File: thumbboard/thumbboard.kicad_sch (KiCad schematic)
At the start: 9 parts, among them J1 Conn_01x05_MountingPin, SW1 SW_Push, SW2 SW_Push, SW3 SW_Push, SW4 SW_Push

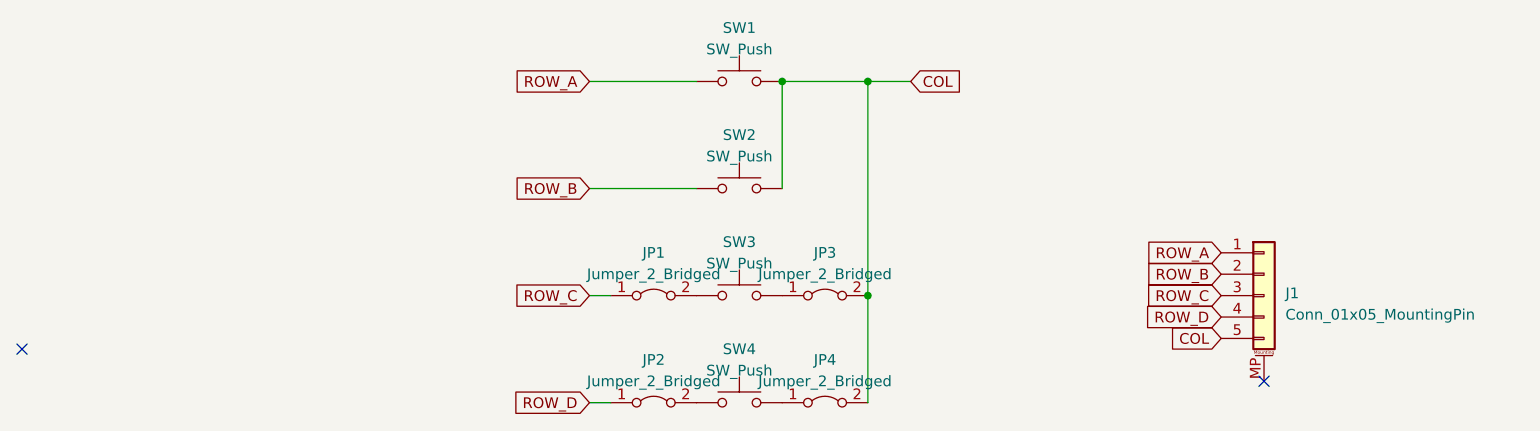
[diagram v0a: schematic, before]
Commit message: layout and cleanups (but J1 still in the wrong spot)
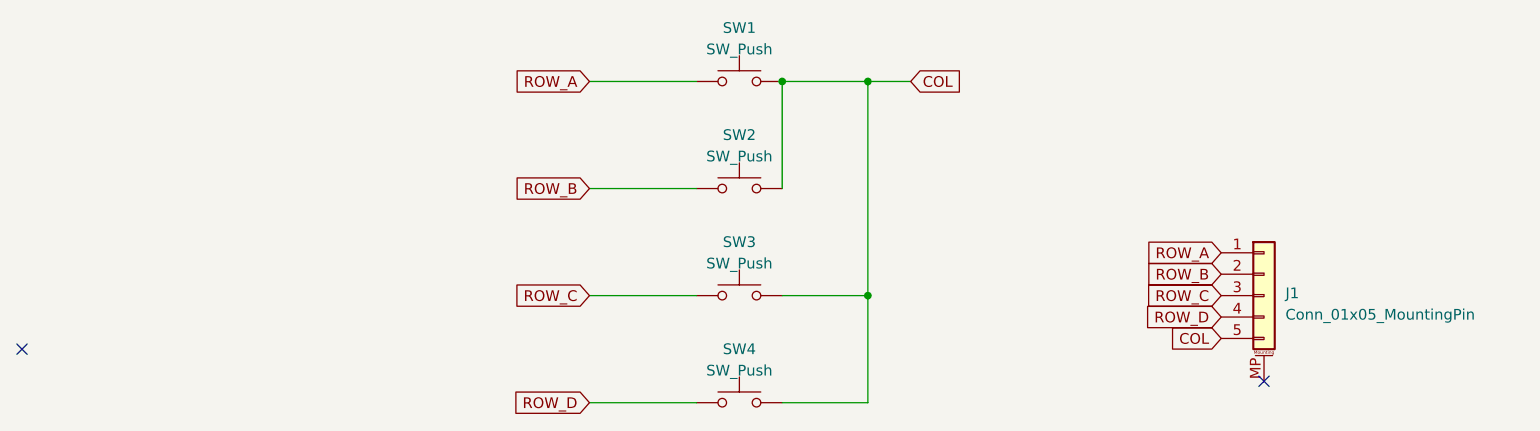
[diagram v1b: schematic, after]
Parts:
- removed JP1, JP2, JP3, JP4: Jumper_2_Bridged, symbol Jumper:Jumper_2_Bridged
- J1: footprint (none) -> Connector_FFC-FPC:Molex_200528-0050_1x05-1MP_P1.00mm_Horizontal
- SW1, SW2, SW3, SW4: footprint (none) -> keyswitches:SW_PG1350
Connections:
- net COL: now also SW1.1, SW3.2, SW4.2; no longer SW1.2
- net ROW_A: now also SW1.2; no longer SW1.1
- net ROW_C: now also SW3.1
- net ROW_D: now also SW4.1
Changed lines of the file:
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@@
     (stroke (width 0) (type default))
   )
-  (wire (pts (xy 88.9 127) (xy 91.44 127))
+  (wire (pts (xy 111.76 127) (xy 121.92 127))
+    (stroke (width 0) (type default))
+  )
+  (wire (pts (xy 111.76 114.3) (xy 121.92 114.3))
+    (stroke (width 0) (type default))
+  )
+  (wire (pts (xy 88.9 114.3) (xy 101.6 114.3))
+    (stroke (width 0) (type default))
+  )
+  (wire (pts (xy 88.9 127) (xy 101.6 127))
     (stroke (width 0) (type default))
   )
@@
   )
   (wire (pts (xy 111.76 88.9) (xy 121.92 88.9))
-    (stroke (width 0) (type default))
-  )
-  (wire (pts (xy 88.9 114.3) (xy 91.44 114.3))
     (stroke (width 0) (type default))
   )
@@
     )
   )
-  (symbol (lib_id "Jumper:Jumper_2_Bridged") (at 96.52 127 0) (unit 1)
-    (in_bom yes) (on_board yes) (dnp no) (fields_autoplaced)
-    (property "Reference" "JP2" (at 96.52 121.92 0)
-      (effects (font (size 1.27 1.27)))
-    )
-    (property "Value" "Jumper_2_Bridged" (at 96.52 124.46 0)
-      (effects (font (size 1.27 1.27)))
-    )
-    (property "Footprint" "" (at 96.52 127 0)
-      (effects (font (size 1.27 1.27)) hide)
-    )
-    (property "Datasheet" "~" (at 96.52 127 0)
-      (effects (font (size 1.27 1.27)) hide)
-    )
-    (pin "1")
-    (pin "2")
-    (instances
-      (project "thumbboard"
-        (path "/7b004c99-6bcb-4fa5-9aa1-9e98c42a949d"
-          (reference "JP2") (unit 1)
-        )
-      )
-    )
-  )
   (symbol (lib_id "Switch:SW_Push") (at 106.68 127 0) (unit 1)
-    (in_bom yes) (on_board yes) (dnp no) (fields_autoplaced)
+    (in_bom yes) (on_board yes) (dnp no)
     (property "Reference" "SW4" (at 106.68 120.65 0)
       (effects (font (size 1.27 1.27)))
@@
       (effects (font (size 1.27 1.27)))
     )
-    (property "Footprint" "" (at 106.68 121.92 0)
+    (property "Footprint" "keyswitches:SW_PG1350" (at 106.68 121.92 0)
       (effects (font (size 1.27 1.27)) hide)
     )
@@
   )
   (symbol (lib_id "Switch:SW_Push") (at 106.68 114.3 0) (unit 1)
-    (in_bom yes) (on_board yes) (dnp no) (fields_autoplaced)
+    (in_bom yes) (on_board yes) (dnp no)
     (property "Reference" "SW3" (at 106.68 107.95 0)
       (effects (font (size 1.27 1.27)))
@@
       (effects (font (size 1.27 1.27)))
     )
-    (property "Footprint" "" (at 106.68 109.22 0)
+    (property "Footprint" "keyswitches:SW_PG1350" (at 106.68 109.22 0)
       (effects (font (size 1.27 1.27)) hide)
     )
@@
     )
   )
-  (symbol (lib_id "Jumper:Jumper_2_Bridged") (at 116.84 127 0) (unit 1)
-    (in_bom yes) (on_board yes) (dnp no) (fields_autoplaced)
-    (property "Reference" "JP4" (at 116.84 121.92 0)
-      (effects (font (size 1.27 1.27)))
-    )
-    (property "Value" "Jumper_2_Bridged" (at 116.84 124.46 0)
-      (effects (font (size 1.27 1.27)))
-    )
-    (property "Footprint" "" (at 116.84 127 0)
-      (effects (font (size 1.27 1.27)) hide)
-    )
-    (property "Datasheet" "~" (at 116.84 127 0)
-      (effects (font (size 1.27 1.27)) hide)
-    )
-    (pin "1")
-    (pin "2")
-    (instances
-      (project "thumbboard"
-        (path "/7b004c99-6bcb-4fa5-9aa1-9e98c42a949d"
-          (reference "JP4") (unit 1)
-        )
-      )
-    )
-  )
   (symbol (lib_id "Connector_Generic_MountingPin:Conn_01x05_MountingPin") (at 168.91 114.3 0) (unit 1)
-    (in_bom yes) (on_board yes) (dnp no) (fields_autoplaced)
+    (in_bom yes) (on_board yes) (dnp no)
     (property "Reference" "J1" (at 171.45 114.0206 0)
       (effects (font (size 1.27 1.27)) (justify left))
@@
       (effects (font (size 1.27 1.27)) (justify left))
     )
-    (property "Footprint" "" (at 168.91 114.3 0)
+    (property "Footprint" "Connector_FFC-FPC:Molex_200528-0050_1x05-1MP_P1.00mm_Horizontal" (at 168.91 114.3 0)
       (effects (font (size 1.27 1.27)) hide)
     )
@@
     )
   )
-  (symbol (lib_id "Switch:SW_Push") (at 106.68 88.9 0) (unit 1)
-    (in_bom yes) (on_board yes) (dnp no) (fields_autoplaced)
+  (symbol (lib_id "Switch:SW_Push") (at 106.68 88.9 0) (mirror y) (unit 1)
+    (in_bom yes) (on_board yes) (dnp no)
     (property "Reference" "SW1" (at 106.68 82.55 0)
       (effects (font (size 1.27 1.27)))
@@
       (effects (font (size 1.27 1.27)))
     )
-    (property "Footprint" "" (at 106.68 83.82 0)
+    (property "Footprint" "keyswitches:SW_PG1350" (at 106.68 83.82 0)
       (effects (font (size 1.27 1.27)) hide)
     )
@@
     )
   )
-  (symbol (lib_id "Jumper:Jumper_2_Bridged") (at 116.84 114.3 0) (unit 1)
-    (in_bom yes) (on_board yes) (dnp no) (fields_autoplaced)
-    (property "Reference" "JP3" (at 116.84 109.22 0)
-      (effects (font (size 1.27 1.27)))
-    )
-    (property "Value" "Jumper_2_Bridged" (at 116.84 111.76 0)
-      (effects (font (size 1.27 1.27)))
-    )
-    (property "Footprint" "" (at 116.84 114.3 0)
-      (effects (font (size 1.27 1.27)) hide)
-    )
-    (property "Datasheet" "~" (at 116.84 114.3 0)
-      (effects (font (size 1.27 1.27)) hide)
-    )
-    (pin "1")
-    (pin "2")
-    (instances
-      (project "thumbboard"
-        (path "/7b004c99-6bcb-4fa5-9aa1-9e98c42a949d"
-          (reference "JP3") (unit 1)
-        )
-      )
-    )
-  )
   (symbol (lib_id "Switch:SW_Push") (at 106.68 101.6 0) (unit 1)
-    (in_bom yes) (on_board yes) (dnp no) (fields_autoplaced)
+    (in_bom yes) (on_board yes) (dnp no)
     (property "Reference" "SW2" (at 106.68 95.25 0)
       (effects (font (size 1.27 1.27)))
@@
       (effects (font (size 1.27 1.27)))
     )
-    (property "Footprint" "" (at 106.68 96.52 0)
+    (property "Footprint" "keyswitches:SW_PG1350" (at 106.68 96.52 0)
       (effects (font (size 1.27 1.27)) hide)
     )
@@
         )
       )
-    )
-  )
-  (symbol (lib_id "Jumper:Jumper_2_Bridged") (at 96.52 114.3 0) (unit 1)
-    (in_bom yes) (on_board yes) (dnp no) (fields_autoplaced)
-    (property "Reference" "JP1" (at 96.52 109.22 0)
-      (effects (font (size 1.27 1.27)))
-    )
-    (property "Value" "Jumper_2_Bridged" (at 96.52 111.76 0)
-      (effects (font (size 1.27 1.27)))
-    )
-    (property "Footprint" "" (at 96.52 114.3 0)
-      (effects (font (size 1.27 1.27)) hide)
-    )
-    (property "Datasheet" "~" (at 96.52 114.3 0)
-      (effects (font (size 1.27 1.27)) hide)
-    )
-    (pin "1")
-    (pin "2")
-    (instances
-      (project "thumbboard"
-        (path "/7b004c99-6bcb-4fa5-9aa1-9e98c42a949d"
-          (reference "JP1") (unit 1)
-        )
-      )

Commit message: more tweaks to thumbboard, incl changing pinout
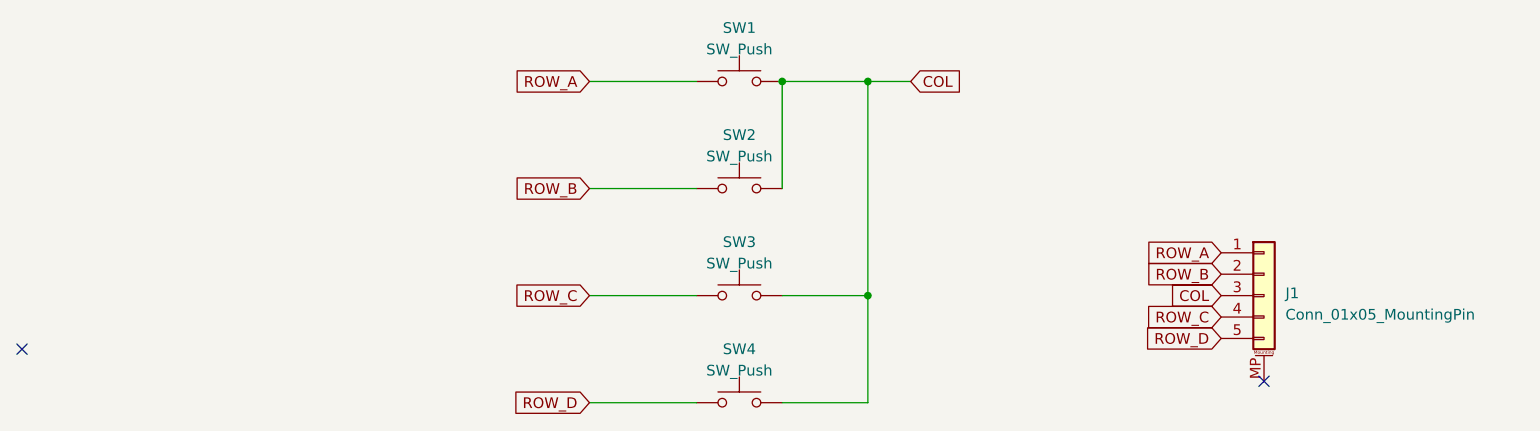
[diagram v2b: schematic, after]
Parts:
- J1: footprint Connector_FFC-FPC:Molex_200528-0050_1x05-1MP_P1.00mm_Horizontal -> Connector_FFC-FPC:TE_84952-5_1x05-1MP_P1.0mm_Horizontal
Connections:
- net COL: now also J1.3 (Pin_3), SW2.1, SW3.1, SW4.1; no longer J1.5 (Pin_5), SW2.2, SW3.2, SW4.2
- net ROW_B: now also SW2.2; no longer SW2.1
- net ROW_C: now also J1.4 (Pin_4), SW3.2; no longer J1.3 (Pin_3), SW3.1
- net ROW_D: now also J1.5 (Pin_5), SW4.2; no longer J1.4 (Pin_4), SW4.1
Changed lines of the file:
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@@
     (stroke (width 0) (type default))
   )
-  (global_label "ROW_D" (shape input) (at 163.83 116.84 180) (fields_autoplaced)
+  (global_label "ROW_D" (shape input) (at 163.83 119.38 180) (fields_autoplaced)
     (effects (font (size 1.27 1.27)) (justify right))
-    (property "Intersheetrefs" "${INTERSHEET_REFS}" (at 154.6347 116.84 0)
+    (property "Intersheetrefs" "${INTERSHEET_REFS}" (at 154.6347 119.38 0)
       (effects (font (size 1.27 1.27)) (justify right) hide)
     )
@@
     )
   )
-  (global_label "ROW_C" (shape input) (at 163.83 114.3 180) (fields_autoplaced)
+  (global_label "ROW_C" (shape input) (at 163.83 116.84 180) (fields_autoplaced)
     (effects (font (size 1.27 1.27)) (justify right))
-    (property "Intersheetrefs" "${INTERSHEET_REFS}" (at 154.6347 114.3 0)
+    (property "Intersheetrefs" "${INTERSHEET_REFS}" (at 154.6347 116.84 0)
       (effects (font (size 1.27 1.27)) (justify right) hide)
     )
   )
-  (global_label "COL" (shape input) (at 163.83 119.38 180) (fields_autoplaced)
+  (global_label "COL" (shape input) (at 163.83 114.3 180) (fields_autoplaced)
     (effects (font (size 1.27 1.27)) (justify right))
-    (property "Intersheetrefs" "${INTERSHEET_REFS}" (at 157.2956 119.38 0)
+    (property "Intersheetrefs" "${INTERSHEET_REFS}" (at 157.2956 114.3 0)
       (effects (font (size 1.27 1.27)) (justify right) hide)
     )
@@
     )
   )
-  (symbol (lib_id "Switch:SW_Push") (at 106.68 127 0) (unit 1)
+  (symbol (lib_id "Switch:SW_Push") (at 106.68 127 0) (mirror y) (unit 1)
     (in_bom yes) (on_board yes) (dnp no)
     (property "Reference" "SW4" (at 106.68 120.65 0)
@@
     )
   )
-  (symbol (lib_id "Switch:SW_Push") (at 106.68 114.3 0) (unit 1)
+  (symbol (lib_id "Switch:SW_Push") (at 106.68 114.3 0) (mirror y) (unit 1)
     (in_bom yes) (on_board yes) (dnp no)
     (property "Reference" "SW3" (at 106.68 107.95 0)
@@
       (effects (font (size 1.27 1.27)) (justify left))
     )
-    (property "Footprint" "Connector_FFC-FPC:Molex_200528-0050_1x05-1MP_P1.00mm_Horizontal" (at 168.91 114.3 0)
+    (property "Footprint" "Connector_FFC-FPC:TE_84952-5_1x05-1MP_P1.0mm_Horizontal" (at 168.91 114.3 0)
       (effects (font (size 1.27 1.27)) hide)
     )
     (property "Datasheet" "~" (at 168.91 114.3 0)
+      (effects (font (size 1.27 1.27)) hide)
+    )
+    (property "Field4" "" (at 168.91 114.3 0)
       (effects (font (size 1.27 1.27)) hide)
     )
@@
     )
   )
-  (symbol (lib_id "Switch:SW_Push") (at 106.68 101.6 0) (unit 1)
+  (symbol (lib_id "Switch:SW_Push") (at 106.68 101.6 0) (mirror y) (unit 1)
     (in_bom yes) (on_board yes) (dnp no)
     (property "Reference" "SW2" (at 106.68 95.25 0)
